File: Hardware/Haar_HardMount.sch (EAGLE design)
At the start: 15 parts, among them J1 CONN_42.54, Q1 2N7002, U1 SHT35DFN, U2 LPS35HW, U4 TPS62237DRY, U5 TXS0102DQM

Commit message: Added HardMount version, improved layout on conventional version
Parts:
- J1: value CONN_42.54 -> SOLDERCUP_CONN_QUAD; device bschulz:CONN_42.54 -> bschulz:SOLDERCUP_CONN_QUAD
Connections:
- net SCL_EXT_HV: now also J1.1; no longer J1.2
- net SDA_EXT_HV: now also J1.2; no longer J1.3
- net VIN+: now also J1.3; no longer J1.4
- net VIN-: now also J1.4; no longer J1.1
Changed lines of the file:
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@@
 <part name="C4" library="bschulz_passives" deviceset="C-EU" device="C0402" technology="0.1UF"/>
 <part name="GND7" library="supply1" library_urn="urn:adsk.eagle:library:371" deviceset="GND" device=""/>
-<part name="J1" library="bschulz" deviceset="CONN_4" device="2.54"/>
+<part name="J1" library="bschulz" deviceset="SOLDERCUP_CONN_QUAD" device=""/>
 <part name="Q1" library="bschulz" deviceset="MOSFET-NCH" device="-2N7002PW" value="2N7002"/>
 <part name="C5" library="bschulz_passives" deviceset="C-EU" device="C0402" technology="0.1UF"/>
@@
 </segment>
 <segment>
-<pinref part="J1" gate="G$1" pin="4"/>
-<wire x1="144.78" y1="48.26" x2="149.86" y2="48.26" width="0.1524" layer="91"/>
-<label x="147.32" y="48.26" size="1.778" layer="95"/>
-</segment>
-<segment>
 <pinref part="Q1" gate="NMOS" pin="G"/>
 <wire x1="180.34" y1="50.8" x2="180.34" y2="53.34" width="0.1524" layer="91"/>
@@
 <wire x1="116.84" y1="116.84" x2="119.38" y2="116.84" width="0.1524" layer="91"/>
 <label x="119.38" y="116.84" size="1.778" layer="95" xref="yes"/>
+</segment>
+<segment>
+<pinref part="J1" gate="G$1" pin="3"/>
+<wire x1="144.78" y1="45.72" x2="149.86" y2="45.72" width="0.1524" layer="91"/>
+<label x="147.32" y="45.72" size="1.778" layer="95"/>
 </segment>
 </net>
@@
 <net name="VIN-" class="0">
 <segment>
+<pinref part="Q1" gate="NMOS" pin="D"/>
+<wire x1="172.72" y1="43.18" x2="167.64" y2="43.18" width="0.1524" layer="91"/>
+<label x="167.64" y="43.18" size="1.778" layer="95" rot="R180" xref="yes"/>
+</segment>
+<segment>
+<pinref part="J1" gate="G$1" pin="4"/>
+<wire x1="144.78" y1="48.26" x2="149.86" y2="48.26" width="0.1524" layer="91"/>
+<label x="147.32" y="48.26" size="1.778" layer="95"/>
+</segment>
+</net>
+<net name="SDA_EXT_HV" class="0">
+<segment>
+<pinref part="U5" gate="G$1" pin="B2"/>
+<wire x1="114.3" y1="106.68" x2="119.38" y2="106.68" width="0.1524" layer="91"/>
+<label x="116.84" y="106.68" size="1.778" layer="95"/>
+</segment>
+<segment>
+<pinref part="J1" gate="G$1" pin="2"/>
+<wire x1="144.78" y1="43.18" x2="149.86" y2="43.18" width="0.1524" layer="91"/>
+<label x="147.32" y="43.18" size="1.778" layer="95"/>
+</segment>
+</net>
+<net name="SCL_EXT_HV" class="0">
+<segment>
+<pinref part="U5" gate="G$1" pin="B1"/>
+<wire x1="114.3" y1="109.22" x2="119.38" y2="109.22" width="0.1524" layer="91"/>
+<label x="116.84" y="109.22" size="1.778" layer="95"/>
+</segment>
+<segment>
 <pinref part="J1" gate="G$1" pin="1"/>
 <wire x1="144.78" y1="40.64" x2="149.86" y2="40.64" width="0.1524" layer="91"/>
 <label x="147.32" y="40.64" size="1.778" layer="95"/>
 </segment>
-<segment>
-<pinref part="Q1" gate="NMOS" pin="D"/>
-<wire x1="172.72" y1="43.18" x2="167.64" y2="43.18" width="0.1524" layer="91"/>
-<label x="167.64" y="43.18" size="1.778" layer="95" rot="R180" xref="yes"/>
-</segment>
-</net>
-<net name="SDA_EXT_HV" class="0">
-<segment>
-<pinref part="J1" gate="G$1" pin="3"/>
-<wire x1="144.78" y1="45.72" x2="149.86" y2="45.72" width="0.1524" layer="91"/>
-<label x="147.32" y="45.72" size="1.778" layer="95"/>
-</segment>
-<segment>
-<pinref part="U5" gate="G$1" pin="B2"/>
-<wire x1="114.3" y1="106.68" x2="119.38" y2="106.68" width="0.1524" layer="91"/>
-<label x="116.84" y="106.68" size="1.778" layer="95"/>
-</segment>
-</net>
-<net name="SCL_EXT_HV" class="0">
-<segment>
-<pinref part="J1" gate="G$1" pin="2"/>
-<wire x1="144.78" y1="43.18" x2="149.86" y2="43.18" width="0.1524" layer="91"/>
-<label x="147.32" y="43.18" size="1.778" layer="95"/>
-</segment>
-<segment>
-<pinref part="U5" gate="G$1" pin="B1"/>
-<wire x1="114.3" y1="109.22" x2="119.38" y2="109.22" width="0.1524" layer="91"/>
-<label x="116.84" y="109.22" size="1.778" layer="95"/>
-</segment>
-</net>
+</net>

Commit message: Fixed ISP error, updated notes
Fixed an errant connection to the ISP header on both versions in schematic, still need to fix the layout. Also removed outdated notes on schematic
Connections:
- net SCL: no longer ISP1.MOSI
- net SDA_EXT: now also ISP1.MOSI
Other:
- note removed: "Add BUCK_MODE!"
- note removed: "Connect RH_INT and RH_RST lines!"
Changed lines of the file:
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@@
 <sheet>
 <plain>
-<text x="55.88" y="63.5" size="1.778" layer="91">MOSI</text>
+<text x="58.42" y="86.36" size="1.778" layer="91">MOSI</text>
 <text x="55.88" y="83.82" size="1.778" layer="91">MISO</text>
 <text x="58.42" y="73.66" size="1.778" layer="91">SCK</text>
 <text x="58.42" y="71.12" size="1.778" layer="91">INT0</text>
-<text x="22.86" y="48.26" size="1.778" layer="91">Connect RH_INT
-and RH_RST lines!</text>
-<text x="96.52" y="63.5" size="1.778" layer="91">Add BUCK_MODE!</text>
 </plain>
 <instances>
@@
 <label x="78.74" y="109.22" size="1.778" layer="95"/>
 </segment>
+<segment>
+<pinref part="ISP1" gate="G$1" pin="MOSI"/>
+<wire x1="40.64" y1="129.54" x2="45.72" y2="129.54" width="0.1524" layer="91"/>
+<label x="43.18" y="129.54" size="1.778" layer="95"/>
+</segment>
 </net>
 <net name="RX" class="0">
@@
 <wire x1="109.22" y1="22.86" x2="114.3" y2="22.86" width="0.1524" layer="91"/>
 <label x="111.76" y="22.86" size="1.778" layer="95"/>
-</segment>
-<segment>
-<pinref part="ISP1" gate="G$1" pin="MOSI"/>
-<wire x1="40.64" y1="129.54" x2="45.72" y2="129.54" width="0.1524" layer="91"/>
-<label x="43.18" y="129.54" size="1.778" layer="95"/>
 </segment>
 </net>
@@
 </drawing>
 <compatibility>
-<note version="6.3" minversion="6.2.2" severity="warning">
-Since Version 6.2.2 text objects can contain more than one line,
-which will not be processed correctly with this version.
-</note>
 <note version="8.2" severity="warning">
 Since Version 8.2, EAGLE supports online libraries. The ids

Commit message: Updated part values, added prelim firmware
Added values to parts for full BoM generation, added preliminary test firmware, consolidation and streamlining to come, simply proof of functionality at the moment
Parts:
- C3, C4, C5: value (none) -> 0.1uF
- L1: value (none) -> 2.2uH
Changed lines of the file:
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@@
 <part name="C1" library="bschulz_passives" deviceset="C-EU" device="C0402" value="4.7uF"/>
 <part name="GND1" library="supply1" library_urn="urn:adsk.eagle:library:371" deviceset="GND" device=""/>
-<part name="L1" library="bschulz" deviceset="INDUCTOR" device="0805"/>
+<part name="L1" library="bschulz" deviceset="INDUCTOR" device="0805" value="2.2uH"/>
 <part name="GND2" library="supply1" library_urn="urn:adsk.eagle:library:371" deviceset="GND" device=""/>
 <part name="C2" library="bschulz_passives" deviceset="C-EU" device="C0402" value="4.7uF"/>
 <part name="GND3" library="supply1" library_urn="urn:adsk.eagle:library:371" deviceset="GND" device=""/>
 <part name="GND4" library="supply1" library_urn="urn:adsk.eagle:library:371" deviceset="GND" device=""/>
-<part name="C3" library="bschulz_passives" deviceset="C-EU" device="C0402" technology="0.1UF"/>
+<part name="C3" library="bschulz_passives" deviceset="C-EU" device="C0402" technology="0.1UF" value="0.1uF"/>
 <part name="GND5" library="supply1" library_urn="urn:adsk.eagle:library:371" deviceset="GND" device=""/>
 <part name="GND6" library="supply1" library_urn="urn:adsk.eagle:library:371" deviceset="GND" device=""/>
-<part name="C4" library="bschulz_passives" deviceset="C-EU" device="C0402" technology="0.1UF"/>
+<part name="C4" library="bschulz_passives" deviceset="C-EU" device="C0402" technology="0.1UF" value="0.1uF"/>
 <part name="GND7" library="supply1" library_urn="urn:adsk.eagle:library:371" deviceset="GND" device=""/>
 <part name="J1" library="bschulz" deviceset="SOLDERCUP_CONN_QUAD" device=""/>
 <part name="Q1" library="bschulz" deviceset="MOSFET-NCH" device="-2N7002PW" value="2N7002"/>
-<part name="C5" library="bschulz_passives" deviceset="C-EU" device="C0402" technology="0.1UF"/>
+<part name="C5" library="bschulz_passives" deviceset="C-EU" device="C0402" technology="0.1UF" value="0.1uF"/>
 <part name="GND8" library="supply1" library_urn="urn:adsk.eagle:library:371" deviceset="GND" device=""/>
 <part name="R1" library="bschulz_passives" deviceset="R-EU_" device="R0402" technology="10K" value="10k"/>

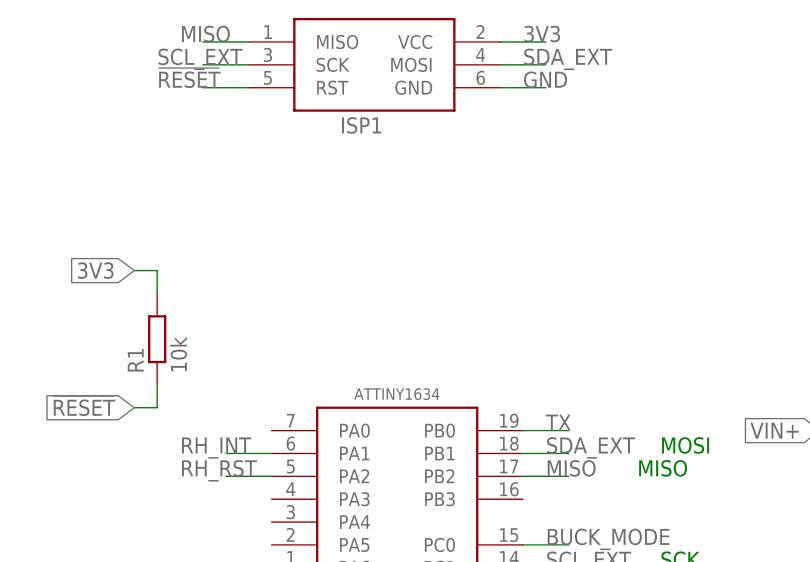
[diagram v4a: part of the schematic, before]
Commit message: Minor cleanup on board, fixed #1, sent v0.1 to fab
Minor board cleanup, added pullup resistors on internal I2C lines, fixed #1 issue
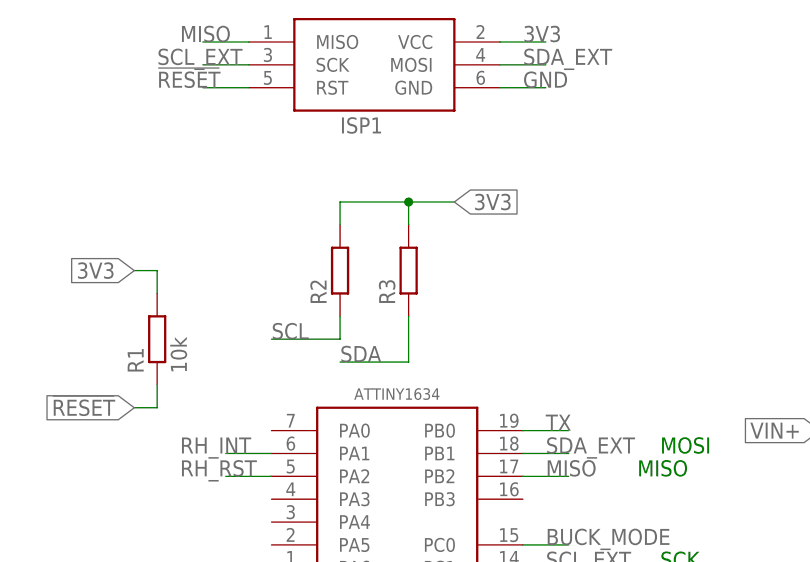
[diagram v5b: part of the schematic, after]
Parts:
- added R2, R3: (no value), bschulz_passives:R-EU_10KR0402
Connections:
- net 3V3: now also R2.2, R3.2
- net SCL: now also R2.1
- net SDA: now also R3.1
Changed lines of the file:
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@@
 <?xml version="1.0" encoding="utf-8"?>
 <!DOCTYPE eagle SYSTEM "eagle.dtd">
-<eagle version="9.2.1">
+<eagle version="9.4.2">
 <drawing>
 <settings>
@@
 <part name="GND9" library="supply1" library_urn="urn:adsk.eagle:library:371" deviceset="GND" device=""/>
 <part name="ISP1" library="bschulz" deviceset="AVRISP" device="1.27MM"/>
+<part name="R2" library="bschulz_passives" deviceset="R-EU_" device="R0402" technology="10K"/>
+<part name="R3" library="bschulz_passives" deviceset="R-EU_" device="R0402" technology="10K"/>
 </parts>
 <sheets>
@@
 <attribute name="NAME" x="22.86" y="121.92" size="1.778" layer="95"/>
 </instance>
+<instance part="R2" gate="G$1" x="22.86" y="106.68" smashed="yes" rot="R90">
+<attribute name="NAME" x="21.3614" y="102.87" size="1.778" layer="95" rot="R90"/>
+<attribute name="VALUE" x="26.162" y="102.87" size="1.778" layer="96" rot="R90"/>
+</instance>
+<instance part="R3" gate="G$1" x="30.48" y="106.68" smashed="yes" rot="R90">
+<attribute name="NAME" x="28.9814" y="102.87" size="1.778" layer="95" rot="R90"/>
+<attribute name="VALUE" x="33.782" y="102.87" size="1.778" layer="96" rot="R90"/>
+</instance>
 </instances>
 <busses>
@@
 <label x="43.18" y="132.08" size="1.778" layer="95"/>
 </segment>
+<segment>
+<pinref part="R2" gate="G$1" pin="2"/>
+<wire x1="22.86" y1="111.76" x2="22.86" y2="114.3" width="0.1524" layer="91"/>
+<wire x1="22.86" y1="114.3" x2="30.48" y2="114.3" width="0.1524" layer="91"/>
+<pinref part="R3" gate="G$1" pin="2"/>
+<wire x1="30.48" y1="114.3" x2="30.48" y2="111.76" width="0.1524" layer="91"/>
+<wire x1="30.48" y1="114.3" x2="35.56" y2="114.3" width="0.1524" layer="91"/>
+<junction x="30.48" y="114.3"/>
+<label x="35.56" y="114.3" size="1.778" layer="95" xref="yes"/>
+</segment>
 </net>
 <net name="SCL_EXT" class="0">
@@
 <label x="111.76" y="25.4" size="1.778" layer="95"/>
 </segment>
+<segment>
+<pinref part="R3" gate="G$1" pin="1"/>
+<wire x1="30.48" y1="101.6" x2="30.48" y2="96.52" width="0.1524" layer="91"/>
+<wire x1="30.48" y1="96.52" x2="22.86" y2="96.52" width="0.1524" layer="91"/>
+<label x="22.86" y="96.52" size="1.778" layer="95"/>
+</segment>
 </net>
 <net name="SCL" class="0">
@@
 <label x="111.76" y="22.86" size="1.778" layer="95"/>
 </segment>
-</net>
+<segment>
+<pinref part="R2" gate="G$1" pin="1"/>
+<wire x1="22.86" y1="101.6" x2="22.86" y2="99.06" width="0.1524" layer="91"/>
+<wire x1="22.86" y1="99.06" x2="15.24" y2="99.06" width="0.1524" layer="91"/>
+<label x="15.24" y="99.06" size="1.778" layer="95"/>
+</segment>
+</net>

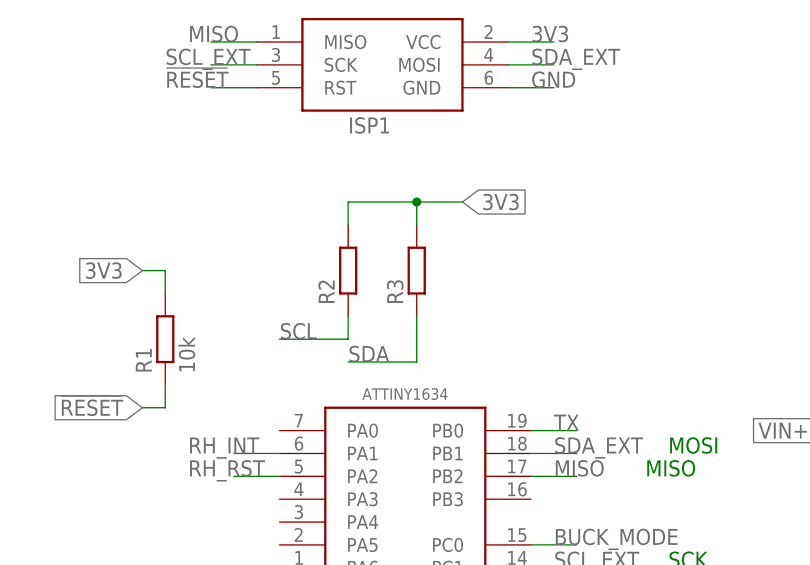
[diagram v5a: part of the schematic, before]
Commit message: Generated fab quote
Updated part values for inductor and capacitor in Eagle, generated new BoM and zipped into file for quote generation
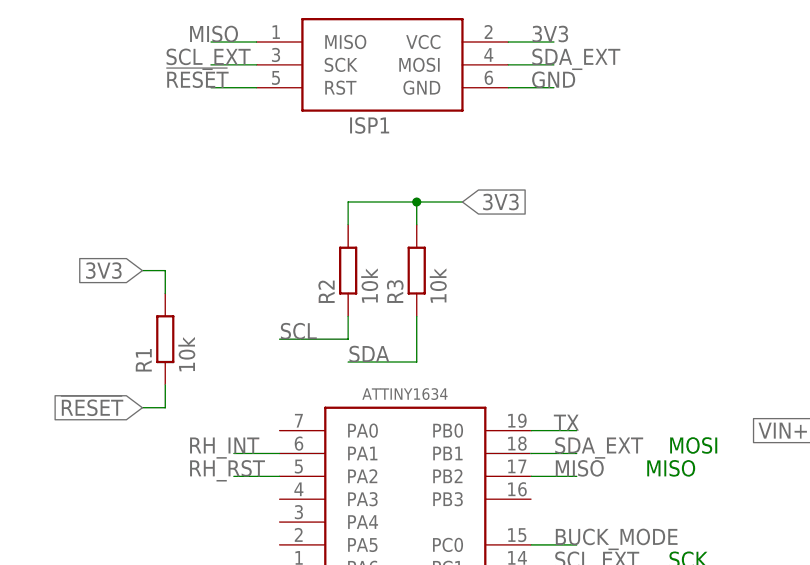
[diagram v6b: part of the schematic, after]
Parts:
- C1, C2: DIGIKEY (none) -> 490-14306-1-ND; MF (none) -> Murata; MPN (none) -> GRM155R61A475MEAAD
- L1: DIGIKEY (none) -> 732-2953-1-ND; MF (none) -> Wurth; MPN (none) -> 74479775222
- R2, R3: value (none) -> 10k
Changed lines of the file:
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@@
 <?xml version="1.0" encoding="utf-8"?>
 <!DOCTYPE eagle SYSTEM "eagle.dtd">
-<eagle version="9.4.2">
+<eagle version="9.5.2">
 <drawing>
 <settings>
@@
 <part name="U3" library="bschulz" deviceset="ATTINY1634" device="QFN"/>
 <part name="U4" library="bschulz" deviceset="TPS6223*" device="DRY" technology="7"/>
-<part name="C1" library="bschulz_passives" deviceset="C-EU" device="C0402" value="4.7uF"/>
+<part name="C1" library="bschulz_passives" deviceset="C-EU" device="C0402" value="4.7uF">
+<attribute name="DIGIKEY" value="490-14306-1-ND"/>
+<attribute name="MF" value="Murata"/>
+<attribute name="MPN" value="GRM155R61A475MEAAD"/>
+</part>
 <part name="GND1" library="supply1" library_urn="urn:adsk.eagle:library:371" deviceset="GND" device=""/>
-<part name="L1" library="bschulz" deviceset="INDUCTOR" device="0805" value="2.2uH"/>
+<part name="L1" library="bschulz" deviceset="INDUCTOR" device="0805" value="2.2uH">
+<attribute name="DIGIKEY" value="732-2953-1-ND"/>
+<attribute name="MF" value="Wurth"/>
+<attribute name="MPN" value="74479775222"/>
+</part>
 <part name="GND2" library="supply1" library_urn="urn:adsk.eagle:library:371" deviceset="GND" device=""/>
-<part name="C2" library="bschulz_passives" deviceset="C-EU" device="C0402" value="4.7uF"/>
+<part name="C2" library="bschulz_passives" deviceset="C-EU" device="C0402" value="4.7uF">
+<attribute name="DIGIKEY" value="490-14306-1-ND"/>
+<attribute name="MF" value="Murata"/>
+<attribute name="MPN" value="GRM155R61A475MEAAD"/>
+</part>
 <part name="GND3" library="supply1" library_urn="urn:adsk.eagle:library:371" deviceset="GND" device=""/>
 <part name="GND4" library="supply1" library_urn="urn:adsk.eagle:library:371" deviceset="GND" device=""/>
@@
 <part name="GND9" library="supply1" library_urn="urn:adsk.eagle:library:371" deviceset="GND" device=""/>
 <part name="ISP1" library="bschulz" deviceset="AVRISP" device="1.27MM"/>
-<part name="R2" library="bschulz_passives" deviceset="R-EU_" device="R0402" technology="10K"/>
-<part name="R3" library="bschulz_passives" deviceset="R-EU_" device="R0402" technology="10K"/>
+<part name="R2" library="bschulz_passives" deviceset="R-EU_" device="R0402" technology="10K" value="10k"/>
+<part name="R3" library="bschulz_passives" deviceset="R-EU_" device="R0402" technology="10K" value="10k"/>
 </parts>
 <sheets>
@@
 <attribute name="NAME" x="134.62" y="87.63" size="1.778" layer="95" rot="R180"/>
 <attribute name="VALUE" x="134.62" y="92.71" size="1.778" layer="96" rot="R180"/>
+<attribute name="DIGIKEY" x="129.54" y="88.9" size="2.54" layer="96" rot="R90" display="off"/>
+<attribute name="MF" x="129.54" y="88.9" size="2.54" layer="96" rot="R90" display="off"/>
+<attribute name="MPN" x="129.54" y="88.9" size="2.54" layer="96" rot="R90" display="off"/>
 </instance>
 <instance part="GND2" gate="1" x="121.92" y="76.2" smashed="yes">
